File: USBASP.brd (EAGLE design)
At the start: 45.7 x 21.6 mm, 25 parts, among them IC1 ATMEGA8, IC2 LD111733, J1 Program, J2 Slow clock, J3 USB, J4 ISP Target, J5 VDD Select, Q1 12 MHz

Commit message: Updates for v1.0 release
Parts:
- removed J5: VDD Select, freetronics-luke:JUMPER_SPDT
- added S1: USB, freetronics-jon:USB-MICROB-MB05PMXX
- C3: value 22p 0604 -> 22p 0603
- F1: value 500mA PTC -> 500mA PTC 1812
- J1: value Program -> Slow clock
- J2: value Slow clock -> Program
- J3: value USB -> VDD Select; device freetronics-jon:USB-MICROB-MB05PMXX -> freetronics-luke:JUMPER_SPDT
- R1: value 10k 0604 -> 10k 0603
- moved J1 16.1 mm to (39.9, 2.73), turned to 180 degrees
- moved J2 16.1 mm to (39.9, 18.9), turned to 0 degrees
- moved J3 12.7 mm to (11.4, 18.8), turned to 180 degrees
- moved C3 1.02 mm to (35.6, 16.8)
- moved C6 0.76 mm to (3.05, 18.1)
- renumbered J4 to S2, Q1 to XTL1
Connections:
- removed net SLOW_SCK: IC1.25, J2.2
- new net SLOW_CLK: IC1.25, J1.2
- net !RESET: now also J2.1; no longer J1.1
- net !RESET_OUT: now also J2.2; no longer J1.2
- net +3V3: now also J3.1; no longer J5.1
- net +5V: now also J3.3; no longer J5.3
- net GND: now also J1.1, S1.FIX1, S1.FIX2, S1.GND, S1.PIN1, S1.PIN2, S1.TAB1, S1.TAB2; no longer J2.1, J3.FIX1, J3.FIX2, J3.GND, J3.PIN1, J3.PIN2, J3.TAB1, J3.TAB2
- net N$141: now also S1.VBUS; no longer J3.VBUS
- net N$143: now also S1.D+; no longer J3.D+
- net N$144: now also S1.D-; no longer J3.D-
- net VDD: now also J3.2; no longer J5.2
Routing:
- net SLOW_SCK: track 7.99 -> 0.00 mm, vias 1 -> 0
- net SLOW_CLK: track 0.00 -> 7.99 mm, vias 0 -> 1
- net VDD: track 99.8 -> 102.6 mm
- net +5V: track 39.7 -> 42.0 mm
- net N$143: track 23.9 -> 23.2 mm
- net +3V3: track 15.4 -> 16.1 mm
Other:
- board text added: "(c) 2013 Freetronics Pty Ltd"
- board text added: "SKU:USBASP"
- board text added: "SLOW CLK"
- board text added: "USBASP AVR Programmer"
- board text added: "VOUT"
- board text added: "www.freetronics.com/usbasp"
- board text removed: "(c) 2012 Freetronics Pty Ltd"
- board text removed: "Copyright 2012 Freetronics Pty Ltd"
- board text removed: "SKU:AVRPROG"
- board text removed: "SLOW CLOCK"
- board text removed: "USB AVR Programmer"
- board text removed: "USBasp AVR Programmer"
- board text removed: "VDD"
- board text removed: "VOLTAGE"
- board text removed: "www.freetronics.com/avrprog"

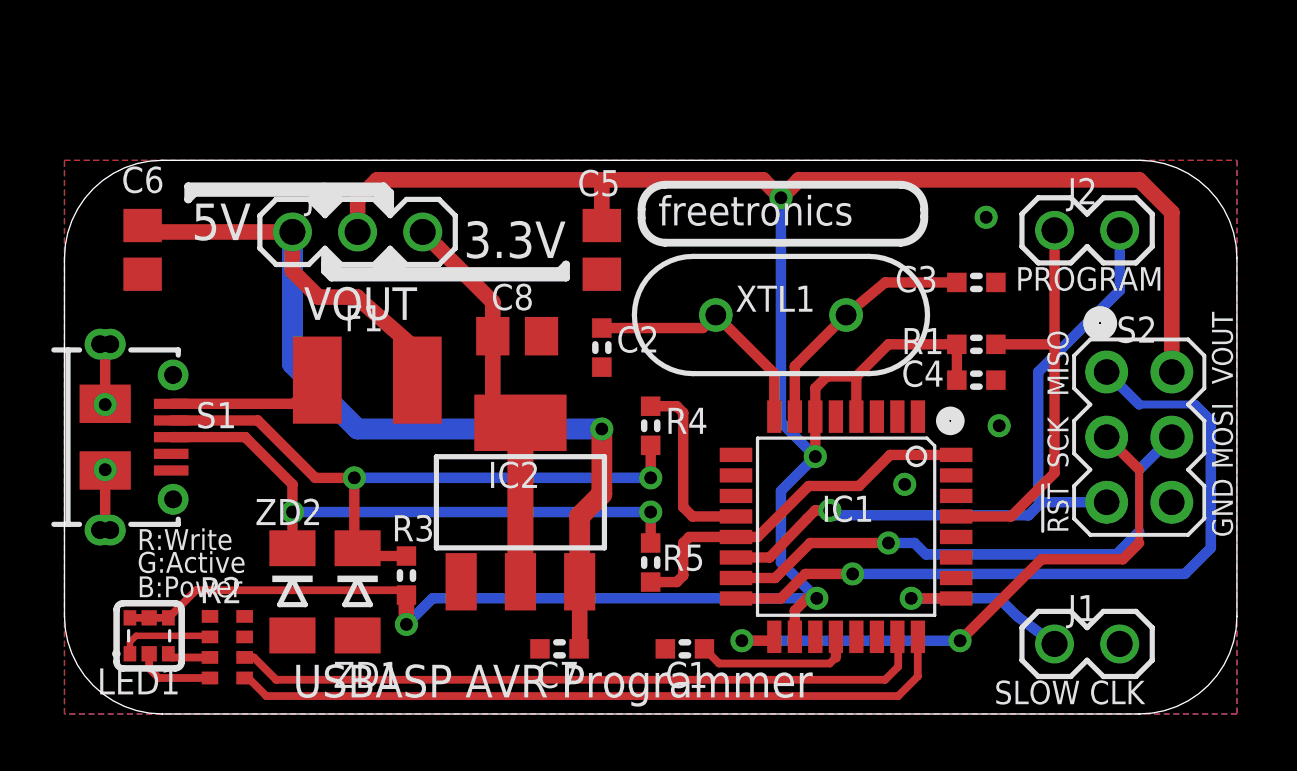
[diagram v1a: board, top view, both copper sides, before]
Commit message: Added jumper to enable / disable target power; improved labels
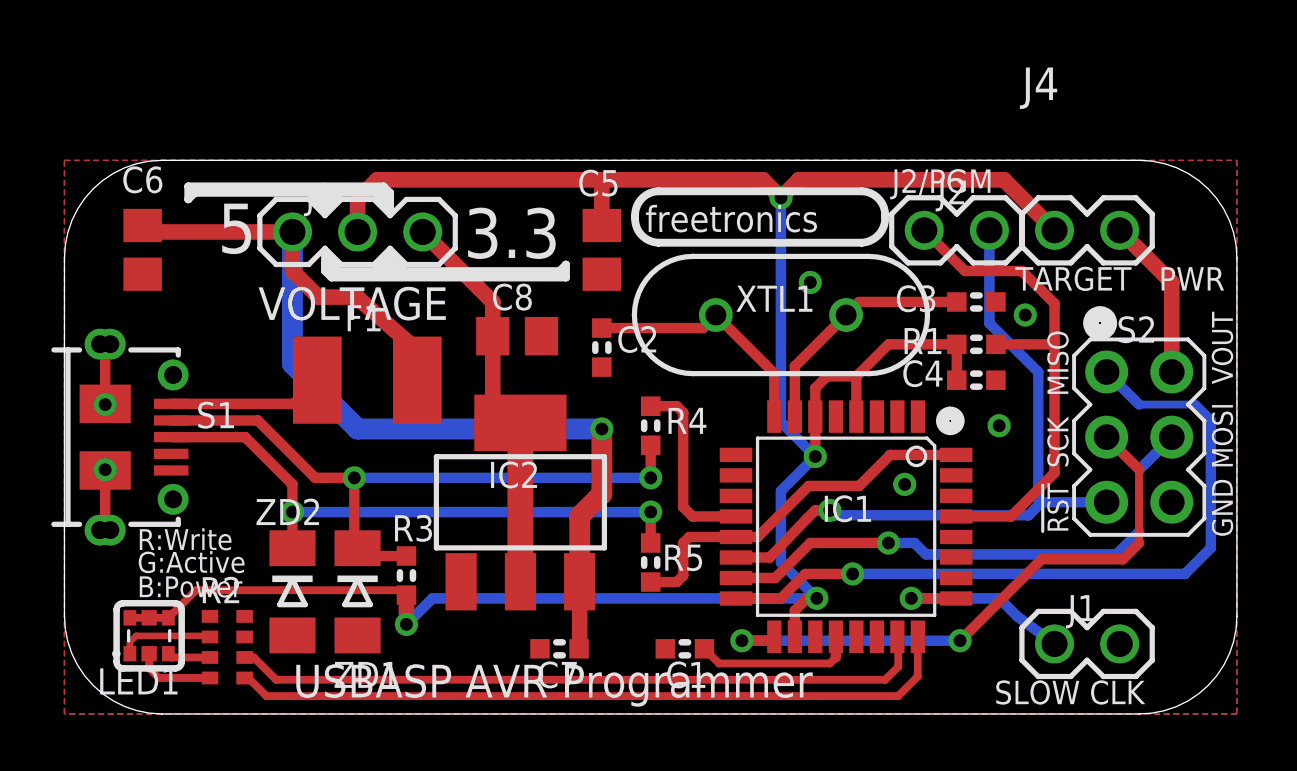
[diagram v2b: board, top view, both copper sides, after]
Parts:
- added J4: Target power, freetronics-luke:HEADER_1X02
- moved J2 5.08 mm to (34.8, 18.9)
- moved C3 0.76 mm to (35.6, 16.1)
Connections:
- new net N$4: J4.2, S2.2
- net VDD: now also J4.1; no longer S2.2
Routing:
- net VDD: track 102.6 -> 92.1 mm
- net N$4: track 0.00 -> 6.37 mm
- net !RESET: track 16.3 -> 19.7 mm
- net !RESET_OUT: track 27.5 -> 27.0 mm
- net GND: vias 5 -> 6
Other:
- board text added: "3.3"
- board text added: "5"
- board text added: "J2/PGM"
- board text added: "PWR"
- board text added: "TARGET"
- board text added: "VOLTAGE"
- board text removed: "3.3V"
- board text removed: "5V"
- board text removed: "PROGRAM"
